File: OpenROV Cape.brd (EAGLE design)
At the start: 71.8 x 54.6 mm, 51 parts, among them IC1 ATMEGA328P-PU, Q1 MOSFET-NCHANNELSMD, Q2 MOSFET-NCHANNELSMD, Q3 MOSFET-NCHANNELSMD, U1 ARDUINO_SHIELDNO_SILK, Y1 16Mhz

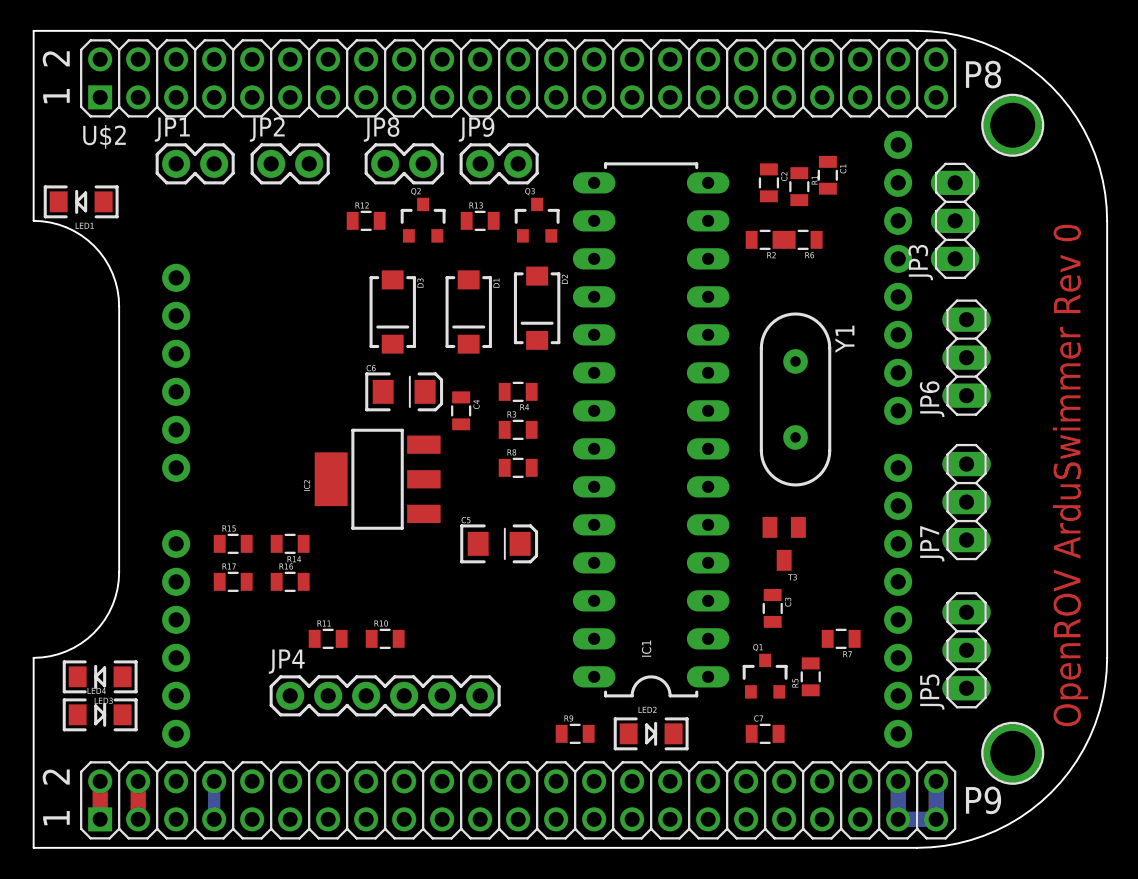
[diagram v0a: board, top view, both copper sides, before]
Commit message: Added values and fixed errors
Added/ corrected values to most components, corrected erroneous voltage
divider configuration to TX-O, added resister between BBTX and RX-I,
changed sheet labels
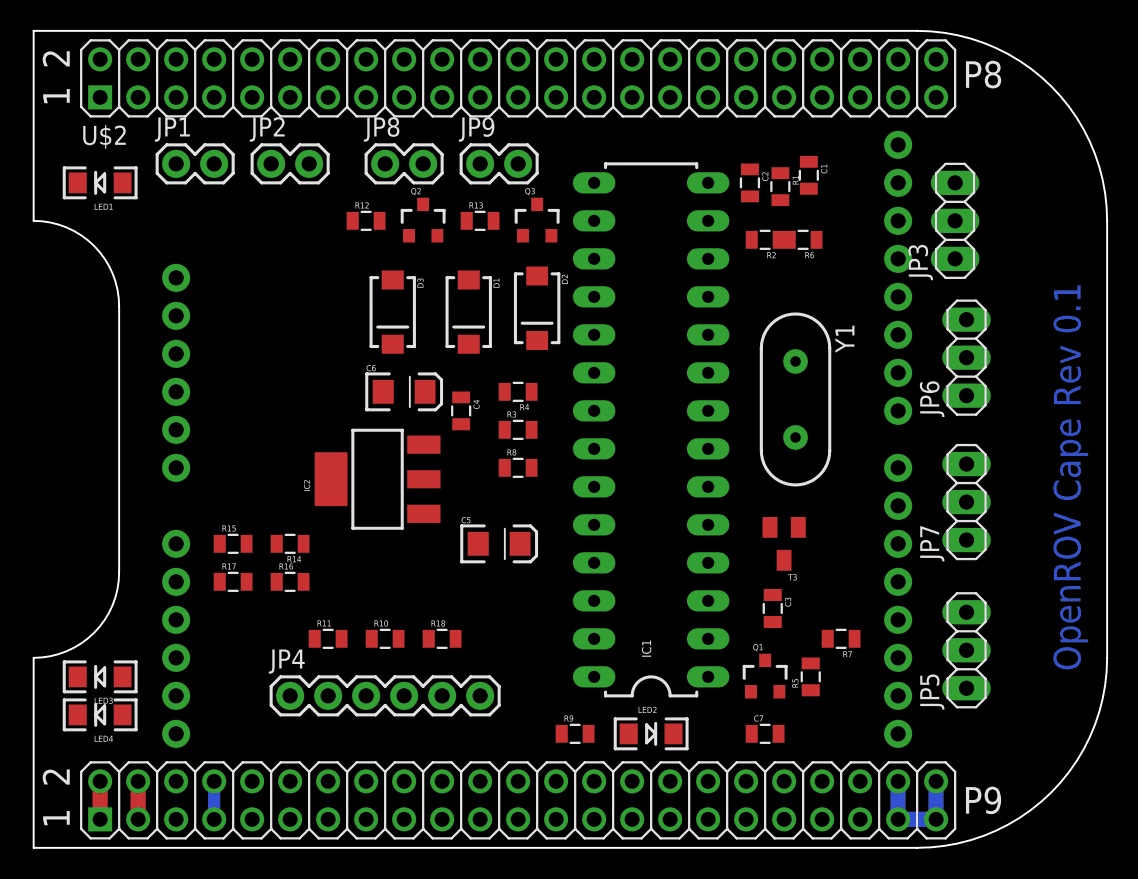
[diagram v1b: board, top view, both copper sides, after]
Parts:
- removed U$22, U$23: MOUNTINGHOLE3.0THIN, microbuilder:MOUNTINGHOLE_3.0_PLATEDTHIN
- added R18: 20k, SparkFun-Passives:0805
- C1, C2: value (none) -> 22pF
- C3: value (none) -> 470uF
- D1, D2: value (none) -> 1N4004
- R1: value (none) -> 33k
- R14: value 100K -> 22k
- R15: value 47K -> 15k
- R16: value 20 -> 20k
- R2: value (none) -> 20k
- R5: value (none) -> 3.3k
- R6: value (none) -> 10k
- R7: value (none) -> 1k
- R9: value (none) -> 330
- T3: value (none) -> 2N2222A
- moved LED1 1.80 mm to (19.1, 44.5)
- moved C1 1.27 mm to (66.4, 45.0)
- moved C2 1.27 mm to (62.5, 44.5)
- moved R1 1.27 mm to (64.5, 44.2)
- turned LED4 to 180 degrees
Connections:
- removed net N$2: R2.2
- new net BBRX: R1.2, R2.2, U$2.72
- new net BBTX: R18.2, U$2.70
- net RX-I: now also R18.1
- net TX-O: no longer R1.2
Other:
- board text added: "OpenROV Cape Rev 0.1"
- board text removed: "OpenROV ArduSwimmer Rev 0"

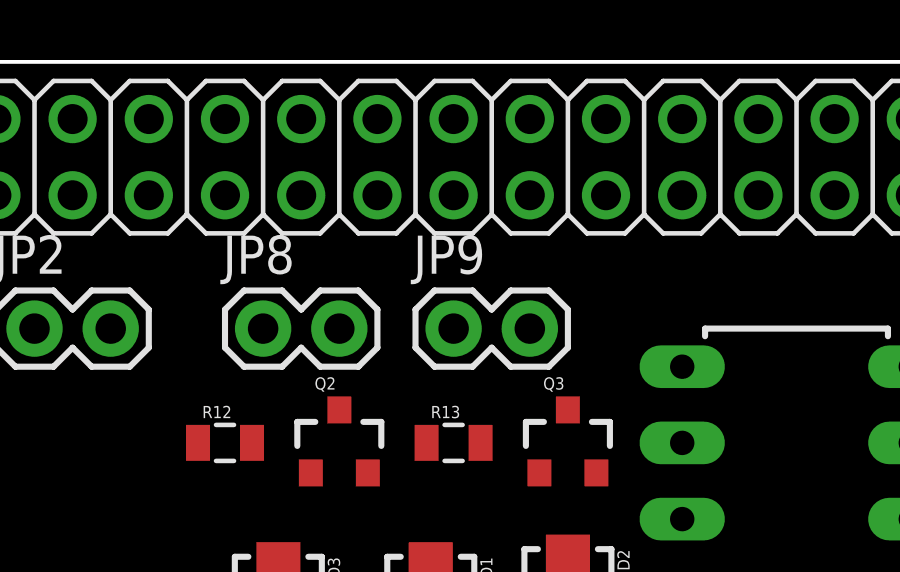
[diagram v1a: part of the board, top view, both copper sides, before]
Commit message: Disambiguated several features
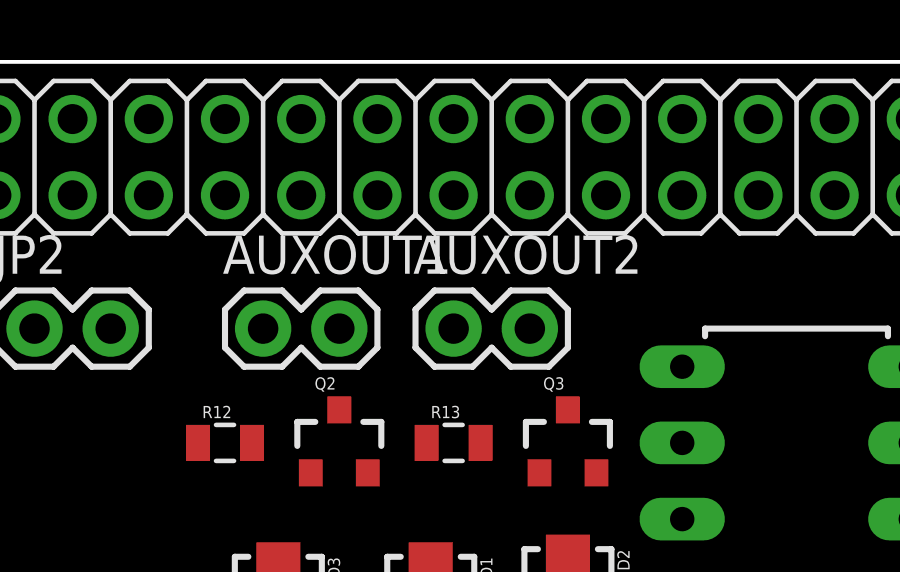
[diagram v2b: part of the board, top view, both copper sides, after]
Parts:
- D3: value (none) -> 1N4004
- JP3: value Camera ESC -> Camera Servo
- R12, R13: value (none) -> 3.3k
- renumbered JP8 to AUXOUT1, JP9 to AUXOUT2
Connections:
- removed net GPIO1_6: U$2.3
- removed net N$6: R7.1
- new net ARDUINORESET: R7.1, U$2.3
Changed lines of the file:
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@@
 <element name="R5" library="SparkFun-Passives" package="0805" value="3.3k" x="66.548" y="11.43" rot="R90"/>
 <element name="C3" library="SparkFun-Passives" package="0805" value="470uF" x="64.008" y="16.002" rot="R270"/>
-<element name="D3" library="SparkFun-DiscreteSemi" package="SMA-DIODE" value="" x="38.608" y="35.814" rot="R270"/>
+<element name="D3" library="SparkFun-DiscreteSemi" package="SMA-DIODE" value="1N4004" x="38.608" y="35.814" rot="R270"/>
 <element name="IC2" library="SparkFun-PowerIC" package="SOT223" value="" x="37.592" y="24.638" rot="R90"/>
 <element name="JP5" library="pinhead" package="1X03" value="Port ESC" x="76.962" y="13.208" rot="R90"/>
@@
 <element name="JP2" library="SparkFun" package="1X02" value="" x="30.48" y="45.72"/>
 <element name="Q1" library="SparkFun-DiscreteSemi" package="SOT23-3" value="MOSFET-NCHANNELSMD" x="63.5" y="11.43"/>
-<element name="JP3" library="pinhead" package="1X03" value="Camera ESC" x="76.2" y="41.91" rot="R90"/>
+<element name="JP3" library="pinhead" package="1X03" value="Camera Servo" x="76.2" y="41.91" rot="R90"/>
 <element name="R3" library="SparkFun-Passives" package="0805" value="720" x="46.99" y="27.94"/>
 <element name="R4" library="SparkFun-Passives" package="0805" value="240" x="46.99" y="30.48" rot="R180"/>
@@
 <element name="LED3" library="SparkFun-LED" package="LED-1206" value="Yellow" x="19.05" y="11.43" rot="R180"/>
 <element name="LED4" library="SparkFun-LED" package="LED-1206" value="Yellow" x="19.05" y="8.89" rot="R180"/>
-<element name="JP8" library="SparkFun" package="1X02" value="" x="38.1" y="45.72"/>
+<element name="AUXOUT1" library="SparkFun" package="1X02" value="" x="38.1" y="45.72"/>
 <element name="Q2" library="SparkFun-DiscreteSemi" package="SOT23-3" value="MOSFET-NCHANNELSMD" x="40.64" y="41.91"/>
-<element name="R12" library="SparkFun-Passives" package="0805" value="" x="36.83" y="41.91"/>
-<element name="JP9" library="SparkFun" package="1X02" value="" x="44.45" y="45.72"/>
+<element name="R12" library="SparkFun-Passives" package="0805" value="3.3k" x="36.83" y="41.91"/>
+<element name="AUXOUT2" library="SparkFun" package="1X02" value="" x="44.45" y="45.72"/>
 <element name="Q3" library="SparkFun-DiscreteSemi" package="SOT23-3" value="MOSFET-NCHANNELSMD" x="48.26" y="41.91"/>
-<element name="R13" library="SparkFun-Passives" package="0805" value="" x="44.45" y="41.91"/>
+<element name="R13" library="SparkFun-Passives" package="0805" value="3.3k" x="44.45" y="41.91"/>
 <element name="R14" library="SparkFun-Passives" package="0805" value="22k" x="31.75" y="20.32" rot="R180"/>
 <element name="R15" library="SparkFun-Passives" package="0805" value="15k" x="27.94" y="20.32"/>
@@
 <contactref element="LED4" pad="C"/>
 <contactref element="LED3" pad="C"/>
-<contactref element="JP8" pad="1"/>
-<contactref element="JP9" pad="1"/>
+<contactref element="AUXOUT1" pad="1"/>
+<contactref element="AUXOUT2" pad="1"/>
 <contactref element="IC1" pad="22"/>
 <contactref element="R15" pad="1"/>
@@
 <wire x1="24.13" y1="33.02" x2="40.6908" y2="24.638" width="0" layer="19" extent="1-1"/>
 </signal>
-<signal name="GPIO1_6">
-<contactref element="U$2" pad="3"/>
-</signal>
 <signal name="GPIO2_8">
 <contactref element="U$2" pad="43"/>
@@
 <contactref element="R7" pad="2"/>
 <wire x1="65.72" y1="21.42" x2="67.68" y2="13.97" width="0" layer="19" extent="1-1"/>
-</signal>
-<signal name="N$6">
-<contactref element="R7" pad="1"/>
 </signal>
 <signal name="BBRX">
@@
 </signal>
 <signal name="N$12">
-<contactref element="JP8" pad="2"/>
+<contactref element="AUXOUT1" pad="2"/>
 <contactref element="Q2" pad="2"/>
 <wire x1="40.64" y1="45.72" x2="41.59" y2="40.91" width="0" layer="19" extent="1-1"/>
@@
 </signal>
 <signal name="N$14">
-<contactref element="JP9" pad="2"/>
+<contactref element="AUXOUT2" pad="2"/>
 <contactref element="Q3" pad="2"/>
 <wire x1="46.99" y1="45.72" x2="49.21" y2="40.91" width="0" layer="19" extent="1-1"/>
@@
 <wire x1="42.81" y1="13.97" x2="46.99" y2="4.445" width="0" layer="19" extent="1-1"/>
 </signal>
+<signal name="ARDUINORESET">
+<contactref element="U$2" pad="3"/>
+<contactref element="R7" pad="1"/>
+<wire x1="21.59" y1="50.165" x2="69.48" y2="13.97" width="0" layer="19" extent="1-1"/>
+</signal>
 </signals>
